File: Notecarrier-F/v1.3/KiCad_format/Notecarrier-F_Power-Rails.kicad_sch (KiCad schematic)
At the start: 28 parts, among them U10 TPS63020DSJR, U11 MAX17225ELT+, U9 TPS62748YFPT

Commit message: Upgrade the four original ports to KiCad 9; fix F v1.3 DRC; document F errata
Notecarrier-A v2.0, -B v2.1, -F v1.3 and -Pi v1.1 were authored in KiCad 7 and
are now upgraded in place (board 20221018 -> 20241229, schematics -> 20250114).
The upgrade is verified lossless on all four:

- every fabrication layer (copper, mask, paste, silk, Edge.Cuts) is
  geometrically identical before and after at 600 dpi, and drill files are
  textually identical;
- schematic netlists are unchanged - same components, same net partitions
  (A 99/114, B 62/87, F 110/166, Pi 46/95);
- kicanvas renders and the RAG extract both still pass.

Zones are NOT refilled - these ports depend on preserved fills.

Notecarrier-F: the board's 54 net-less 0.6 mm copper patches (footprint
weird-no-fill-via_Fv1.2) sit inside GND copper and are now assigned the GND net
they belong to. DRC goes from 171 errors to 0 with no change to any copper
geometry.

Notecarrier-F ERRATA.md (new): the power section does not match the shipped
board. U9 (AP2139AK-3.3 LDO) with C33/C34, and DS7 (STPS3H100U), are missing
from both schematic and board though they are in the Altium source, the released
BOM, the released pick-and-place, and the shipped copper/mask/paste. All six
diodes carry the wrong part and package: the released design uses FSV1045V in
TO277-3 (3 pads) for DS1/DS2/DS4/DS5 and STPS3H100U in SMB for DS3/DS6/DS7,
where the port has B360A-13-F in DO-214AC SMA (2 pads) throughout. The errata
records the exact wiring and coordinates needed to fix it. Flagged in the root
README and the port's README.

Also documented per port: the DRC exclusions recorded by KiCad 7 no longer
suppress anything, because KiCad 9 computes different marker keys. They are left
as the author's record and the remaining violations are explained in each
Porting-Notes - including evidence that A's J9 pad-vs-zone reports are
preserved-fill artifacts (its In1 plane matches the shipped GND film to within
0.9% of lit area), and that B's 4 error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
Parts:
- renumbered C42 to C16, C42 to C17, C39 to C18, C37 to C19, C36 to C20, C36 to C21, C34 to C22, C35 to C23, C36 to C24, C37 to C25, C37 to C26, C36 to C27, C45 to C28, C36 to C29, C37 to C30, C38 to C31, C37 to C32, DS2 to DS5, L6 to L1, L5 to L2, L4 to L3, R26 to R13, R25 to R14, R27 to R17, R24 to R19, U10 to U3, U11 to U7, U9 to U8

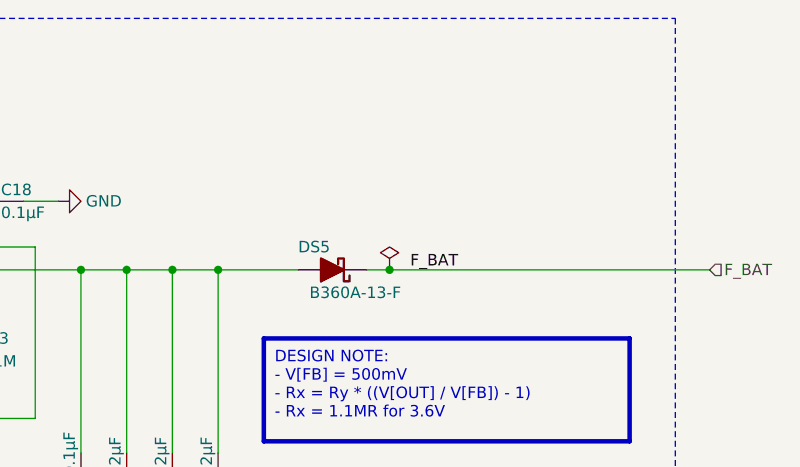
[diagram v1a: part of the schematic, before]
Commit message: Notecarrier-F: apply the v1.2 -> v1.3 schematic delta
The schematic sheets now describe v1.3. Every step was verified by re-exporting
the netlist and comparing against the intended result rather than by
inspection, and the final state is tabulated in ERRATA.md.

- Adds U9 (AP2139AK-3.3TRG1 LDO) with C33/C34, wired as the released schematic
  draws it: VIN and CE both on the DS5 anode node, VOUT on the new F_VIO rail,
  NC left open with a no-connect marker.
- Migrates the six F_VIO nodes off F_BAT (U4.7, C14.1, U1.3, C11.1, R11.2,
  R12.2), leaving F_BAT with only DS5's cathode and the Feather BAT pin. This is
  the substance of the revision: both level shifters previously took their
  Feather-side supply from raw battery voltage.
- Adds DS7 (STPS3H100U) as the Notecard USB input diode.
- Re-parts the six diodes: DS1/DS2/DS4/DS5 to the 3-pin FSV1045V in TO277-3,
  DS3/DS6 to STPS3H100U in SMB.
- Marks R11/R12 DNP rather than deleting them, matching how the released
  schematic strikes them through, and adds a power_F_VIO symbol to the
  project-local library.

Three things did not go as the plan assumed, and the plan was wrong rather than
the files:

- The F_BAT net is four separate wire nodes unified by name, not one, and the
  node carrying C14.1/U4.7 was named by a plain local label sitting mid-wire
  that a hierarchical-label search does not see. Found by probing each naming
  object and re-exporting; no wire surgery turned out to be necessary.
- DS2 alone carries a lib_name override pinning it to a cached 2-pin symbol, so
  changing its lib_id silently did nothing. The netlist check caught it; every
  other diode was fine.
- MODL1/MODR1 cannot be renamed to the released MOD1L/MOD1R. KiCad takes the
  annotation number from a reference's trailing digits, so a name ending in a
  letter reads as unannotated and the exported BOM literally says "MOD1L?".
  Reverted, with the mapping to the released BOM documented instead.

The board still describes v1.2, so the sche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
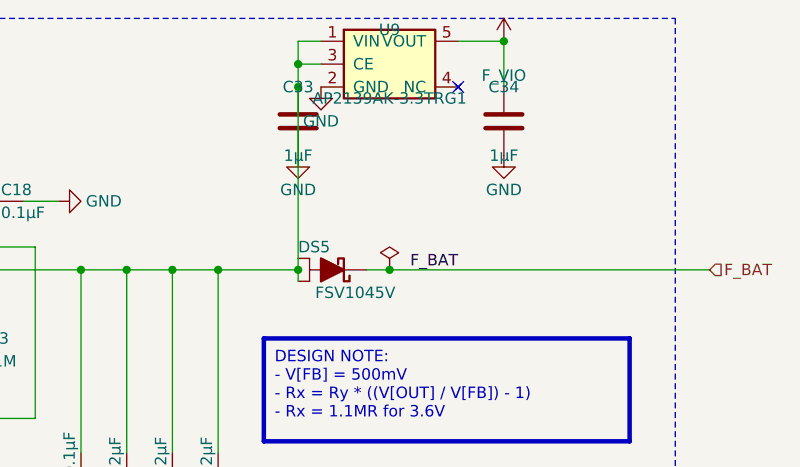
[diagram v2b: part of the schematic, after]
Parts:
- added C33, C34: 1µF, blues-kicad-lib:C-0603_Fv1.2, symbol Device:C
- added U9: AP2139AK-3.3TRG1, Notecarrier-F-local:SOT-23-5_Fv1.3, symbol Notecarrier-F-local:AP2139AK-3.3TRG1
- DS5: value B360A-13-F -> FSV1045V; footprint blues-kicad-lib:DO-214AC SMA_Fv1.2 -> blues-kicad-lib:TO277-3; symbol blues-kicad-lib:D_Schottky_Filled_Swapped -> blues-kicad-lib:FSV1045V; Design Description Schottky Diode B360-13-F 60V/3A -> Schottky Diode FSV1045V 45V/10A; Design MPN B360A-13-F -> FSV1045V; Design Manufacturer Diodes Inc -> onsemi; Design Order Code B360A-FDICT-ND -> (none); Design Supplier Digi-Key -> (none); MPN B360A-13-F -> FSV1045V; Manufacturer Diodes Inc. -> onsemi; Mfr Description Rectifier Diode, Schottky, 1 Phase, 1 Element, 3A, 60V V(RR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 -> Rectifier Diode, Schottky, 1 Phase, 1 Element, 10A, 45V V(R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
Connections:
- net F_BAT: now also DS5.3 (C); no longer DS5.2 (K)
- net GND: now also C33.2, C34.2, U9.2 (GND)
- net at C22.1, C23.1, C24.1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: now also DS5.2 (A2), C33.1, U9.1 (VIN), U9.3 (CE)
- new net F_VIO: C34.1, U9.5 (VOUT)
- no-connect marks 2 -> 3
